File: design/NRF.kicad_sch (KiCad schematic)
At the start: 18 parts, among them J2 Conn_Coaxial, U4 nRF24L01P, X2 16MHz

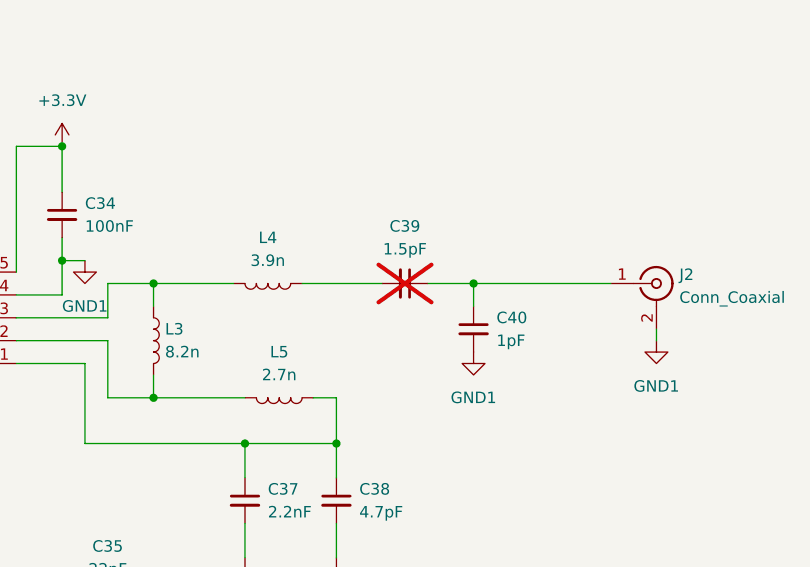
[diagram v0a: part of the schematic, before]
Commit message: Empiezo a ubicar componentes en PCB
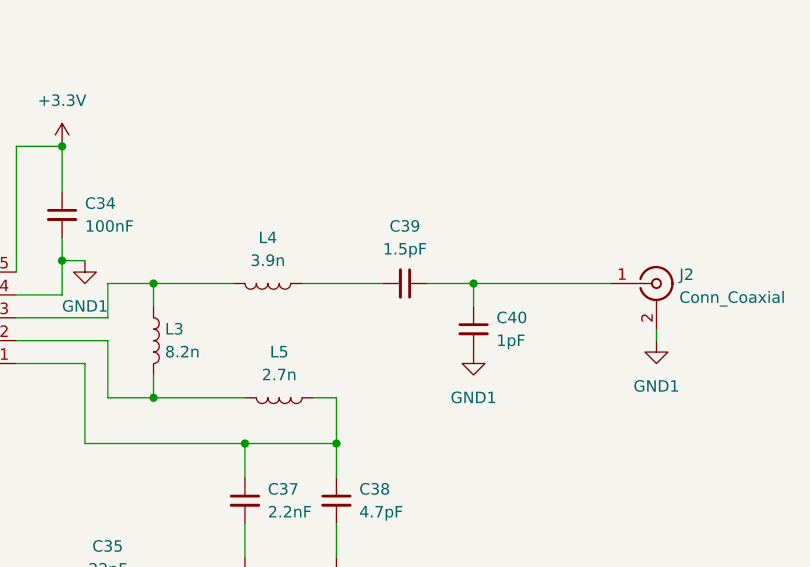
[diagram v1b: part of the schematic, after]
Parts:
- C39: now fitted
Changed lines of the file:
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@@
 		(in_bom yes)
 		(on_board yes)
-		(dnp yes)
+		(dnp no)
 		(fields_autoplaced yes)
 		(property "Reference" "C39"

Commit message: Agrego MFR# de conectores
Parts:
- C39: now not fitted
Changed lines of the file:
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@@
 		(in_bom yes)
 		(on_board yes)
-		(dnp no)
+		(dnp yes)
 		(fields_autoplaced yes)
 		(property "Reference" "C39"
